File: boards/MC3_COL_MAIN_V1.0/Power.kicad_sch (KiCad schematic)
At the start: 6 parts, among them J3 SUPPLY_IN, Q1 AO4407C, U3 AMS1117-3.3

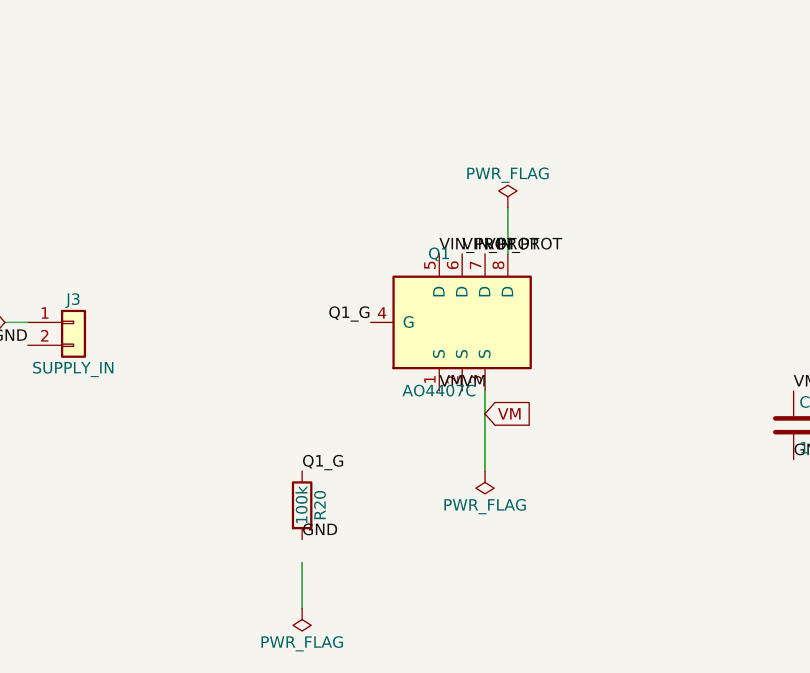
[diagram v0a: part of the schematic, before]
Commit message: Schematic: root sheet on-grid, I2C address straps as GND/+3V3 global labels, ERC clean (warnings only)
- Root: Power/MCU/Connectors + 4x MotorChannel instances on the 1.27 mm grid; sheet pins wired
  to EN/PH/IPROPI/RC_OUT/nFAULT_leafN global labels; A1/A0 straps leaf1 GND/GND, leaf2
  GND/+3V3, leaf3 +3V3/GND, leaf4 +3V3/+3V3 (PROVISIONAL)
- Connectors: removed a GND drop that shorted ENC_leaf4; VM on the FFCs as global labels
- Power: PWR_FLAGs placed on the pin ends (VIN_PROT, VM, GND)
- ERC (kicad-cli, all severities): 0 errors, 8 same_local_global_label warnings (intended)
- Reference designators still duplicated across the 4 channel instances: needs Annotate
  in eeschema (no CLI path)

Co-Authored-By: Claude Fable 5 <noreply@anthropic.com>
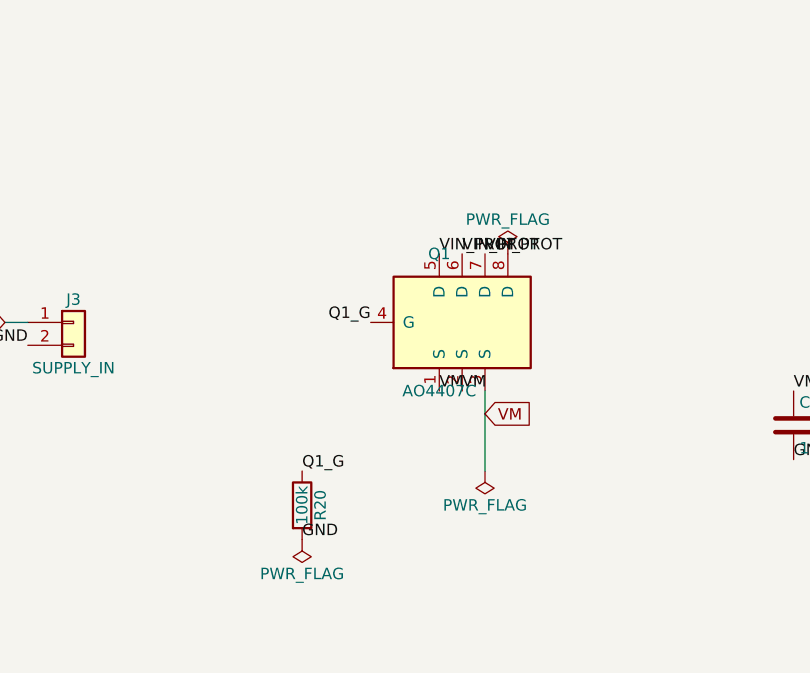
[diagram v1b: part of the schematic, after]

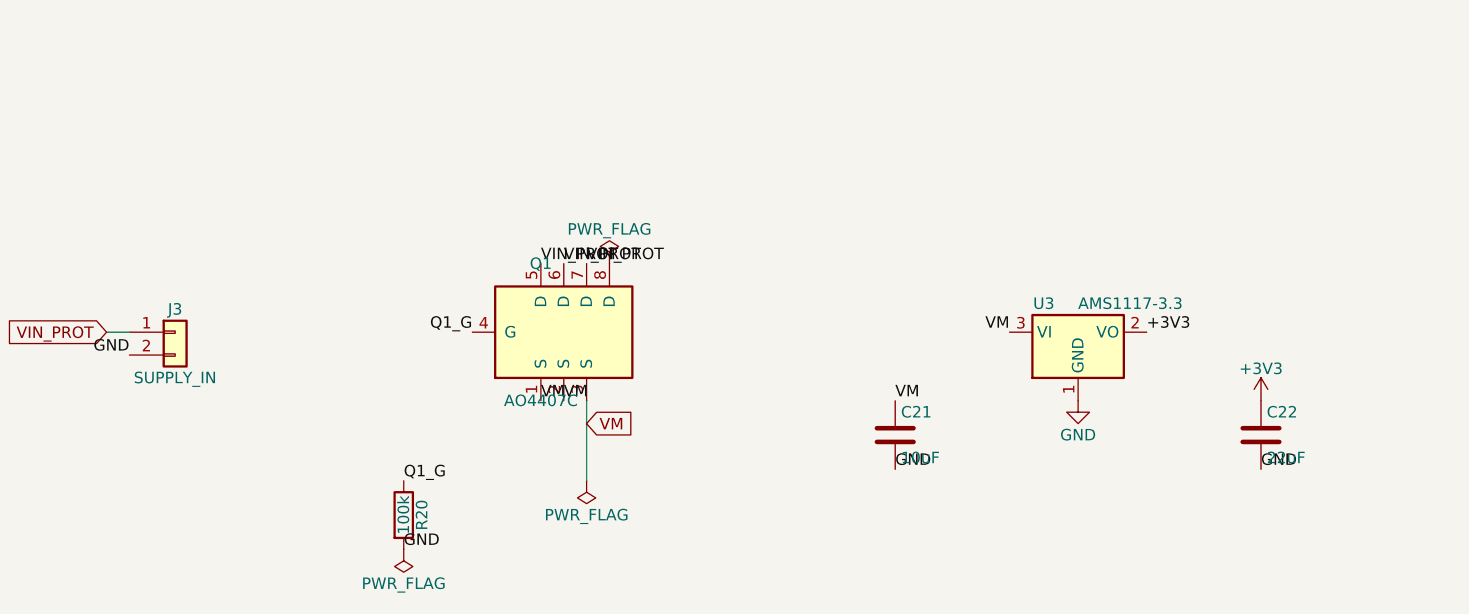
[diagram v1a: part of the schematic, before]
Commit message: Schematic annotated in eeschema (per-instance references for the 4 channel sheets); user review OK
Co-Authored-By: Claude Fable 5 <noreply@anthropic.com>
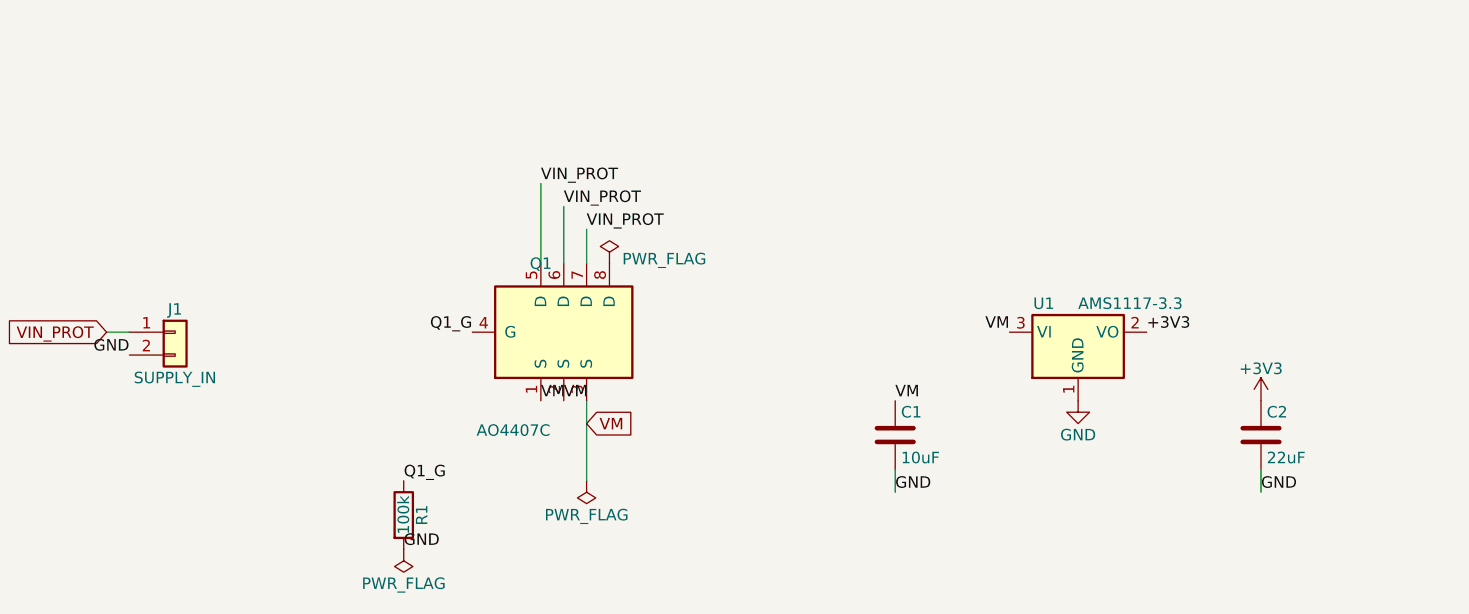
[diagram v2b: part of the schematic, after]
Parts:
- renumbered C21 to C1, C22 to C2, J3 to J1, R20 to R1, U3 to U1

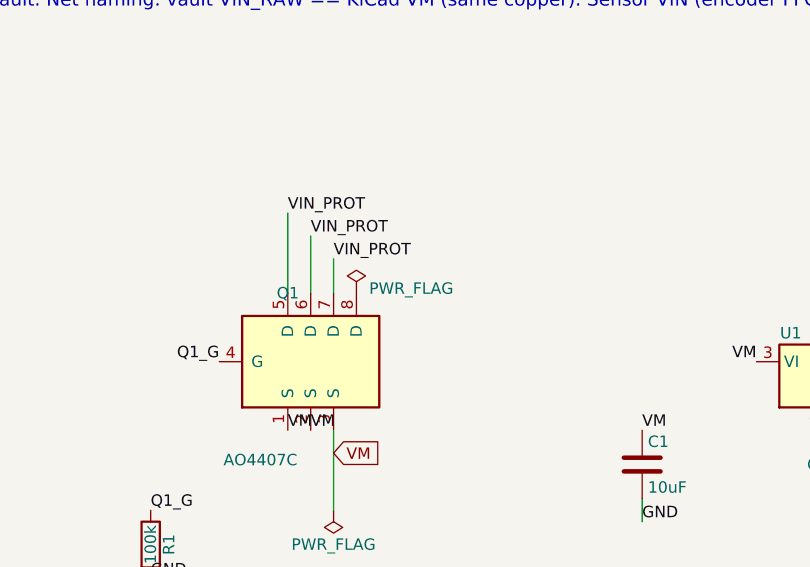
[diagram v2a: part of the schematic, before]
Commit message: Yaw channel fitted as 5th MotorChannel instance (user decision); Power VIN_PROT pin 8 labelled; MIGRATION status
- MCU: EN_yaw PA9, PH_yaw PB12, IPROPI_yaw PC4 (vault reserved pins); PROVISIONAL nFAULT_yaw
  PC12, RC_OUT_yaw PB13
- Root: sheet 'yaw' -> MotorChannel.kicad_sch, A1 open (Hi-Z), A0 GND
- ERC: 0 errors, same_local_global_label warnings only
- Needs re-annotation in eeschema for the new instance

Co-Authored-By: Claude Fable 5 <noreply@anthropic.com>
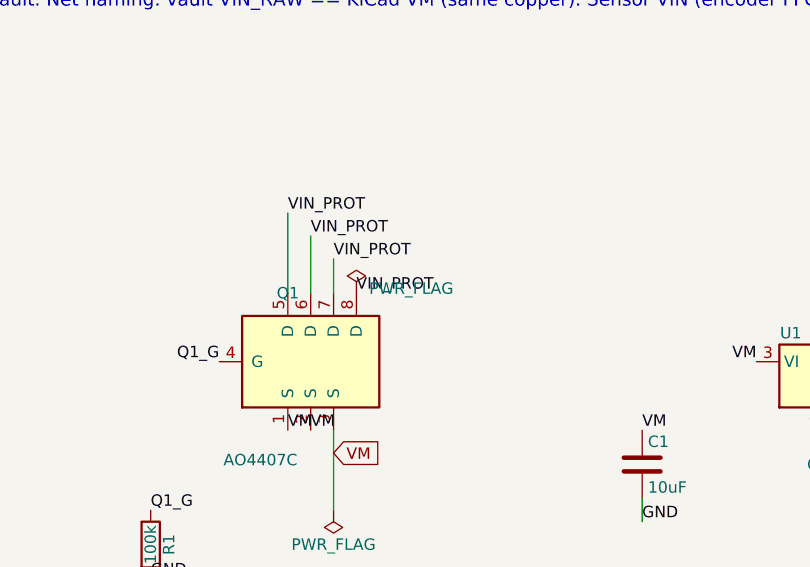
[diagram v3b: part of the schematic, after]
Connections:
- net VIN_PROT: now also Q1.8 (D)
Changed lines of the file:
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@@
 		)
 	)
+  (label "VIN_PROT"
+    (at 87.63000000000001 72.39 0)
+    (fields_autoplaced yes)
+    (effects (font (size 1.27 1.27)) (justify left bottom))
+  )
 	(symbol
 		(lib_id "Regulator_Linear:AMS1117-3.3")

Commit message: I2C address straps: high straps via 2.2k pull-ups R40-R43 (SLVSH04 Table 8-28 note); address table on root sheet
Co-Authored-By: Claude Fable 5 <noreply@anthropic.com>
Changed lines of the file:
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@@
+		)
+	)
+	(label "VIN_PROT"
+		(at 87.63 72.39 0)
+		(effects
+			(font
+				(size 1.27 1.27)
+			)
+			(justify left bottom)
 		)
 	)
@@
 		)
 	)
-  (label "VIN_PROT"
-    (at 87.63000000000001 72.39 0)
-    (fields_autoplaced yes)
-    (effects (font (size 1.27 1.27)) (justify left bottom))
-  )
 	(symbol
 		(lib_id "Regulator_Linear:AMS1117-3.3")

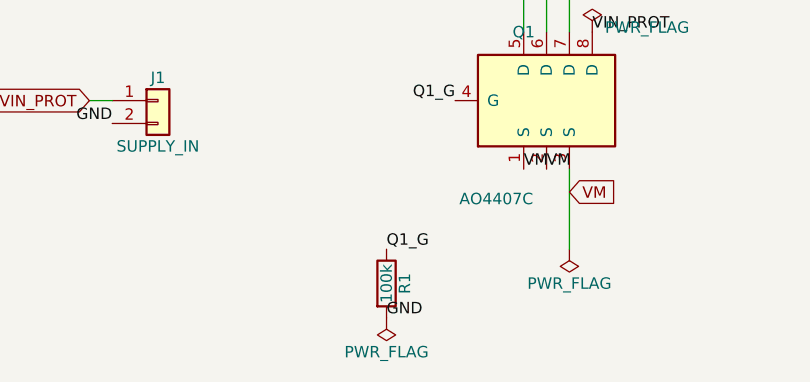
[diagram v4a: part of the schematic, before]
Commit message: Schematic re-annotated in eeschema after yaw channel + strap pull-ups
Co-Authored-By: Claude Fable 5 <noreply@anthropic.com>
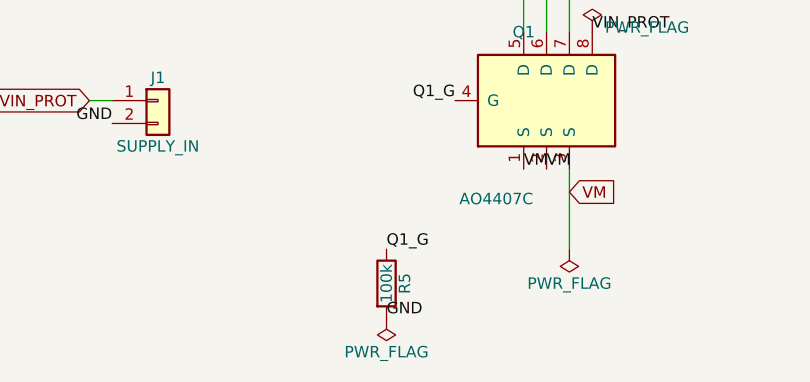
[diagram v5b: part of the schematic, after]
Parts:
- renumbered R1 to R5
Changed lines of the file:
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@@
 		(in_pos_files yes)
 		(dnp no)
-		(property "Reference" "R1"
+		(property "Reference" "R5"
 			(at 66.802 100.33 90)
 			(show_name no)
@@
 			(project "MC3_COL_MAIN_V1.0"
 				(path "/7d5f4202-d55e-4c7b-a2df-dd599db38e48/d6d9c27b-d616-4172-a586-88c2a3452975"
-					(reference "R1")
+					(reference "R5")
 					(unit 1)
 				)

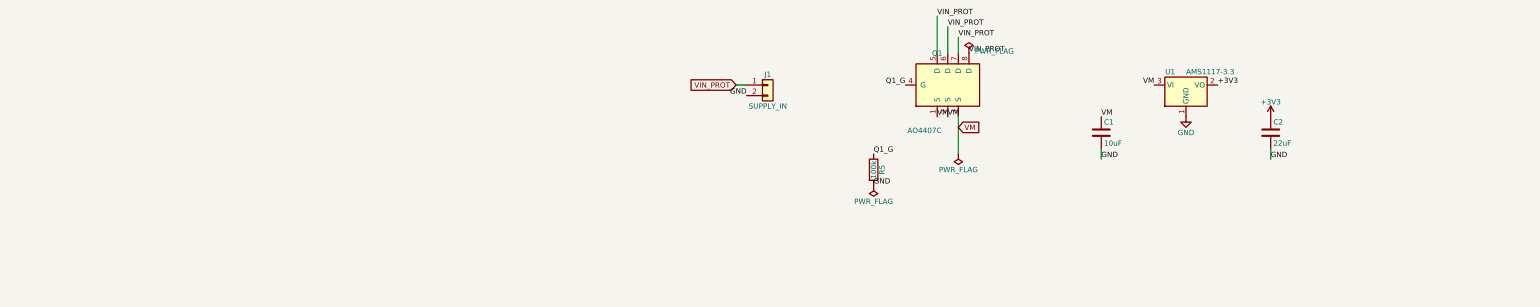
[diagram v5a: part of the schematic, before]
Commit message: Design review changes: HSE caps 33pF, R_IPROPI 6.8k (1.99 A trip), VM bulk, sensor rail filter, input fuse+TVS, NRST cap, 6-pin SWD with SWO, VDDA ferrite, LEDs, test points, tantalum LDO cap
- MCU: C6/C10 18pF -> 33pF (X32258MSB4SI is CL=20pF); C60 100nF on NRST; J2 -> Conn_01x06
  (+NRST, +SWO on PB3); VDDA split from +3V3 through FB60 + PWR_FLAG; heartbeat LED D60/R60
  on PA5, power LED D61/R61; test points TP60-64 (+3V3, SCL, SDA, IPROPI_leaf1, GND)
- Power: J1 -> VIN_PAD -> F60 polyfuse -> VIN_PROT; D62 SMAJ5.0A TVS VIN_PROT-GND; C61/C62
  2x22uF VM bulk; TP65 VM, TP66 VIN_PROT; C2 LDO output cap -> tantalum 22uF 10V (C_Polarized,
  CP_EIA-3216-18)
- Connectors: FFC VIN now VSENS = VM through FB61 + C63 4.7uF
- MotorChannel: R_IPROPI 8.45k -> 6.8k (I_TRIP = 3.3/(6.8k*244uA/A) = 1.99 A)
- Library: stock L_0603, D_SMA, Fuse_1206, CP_EIA-3216-18, TestPoint_Pad_1.0x1.0mm, LED_0603,
  PinHeader_1x06 footprints copied in
- ERC 0 errors (same_local_global_label warnings only); netlist walked

Co-Authored-By: Claude Fable 5 <noreply@anthropic.com>
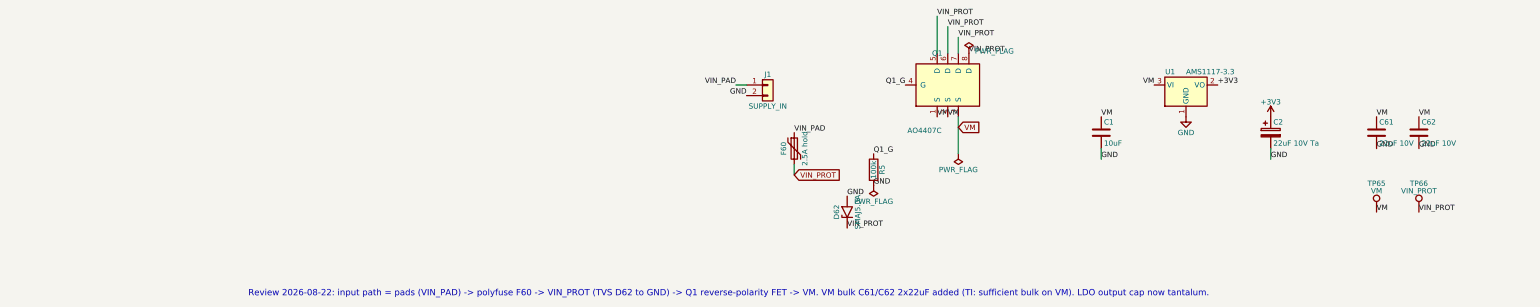
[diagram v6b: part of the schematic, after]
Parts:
- added C61, C62: 22uF 10V, MC3_COL_MAIN:C_0805_2012Metric, symbol Device:C
- added D62: SMAJ5.0A, MC3_COL_MAIN:D_SMA, symbol Diode:SMAJ5.0A
- added F60: 2.5A hold, MC3_COL_MAIN:Fuse_1206_3216Metric, symbol Device:Polyfuse
- added TP65: VM, MC3_COL_MAIN:TestPoint_Pad_1.0x1.0mm, symbol Connector:TestPoint
- added TP66: VIN_PROT, MC3_COL_MAIN:TestPoint_Pad_1.0x1.0mm, symbol Connector:TestPoint
- C2: value 22uF -> 22uF 10V Ta; footprint MC3_COL_MAIN:C_0805_2012Metric -> MC3_COL_MAIN:CP_EIA-3216-18_Kemet-A; symbol Device:C -> Device:C_Polarized; Note LDO output 22uF - AMS1117 compensation cap. OPEN (vault): d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 -> LDO output cap changed to TANTALUM 22uF 10V case A (3216) p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
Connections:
- net GND: now also C61.2, C62.2, D62.2 (A2)
- net VIN_PROT: now also D62.1 (A1), F60.2, TP66.1; no longer J1.1 (Pin_1)
- net VM: now also C61.1, C62.1, TP65.1
- new net VIN_PAD: F60.1, J1.1 (Pin_1)
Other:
- note added: "Review 2026-08-22: input path = pads (VIN_PAD) -> polyfuse F60 -> VIN_PROT (TVS D62 to GND) -> Q1 reverse-polarity FET -> VM. VM bulk C61/C62 2x22uF added (TI: sufficient bulk on VM). LDO output cap now tantalum."

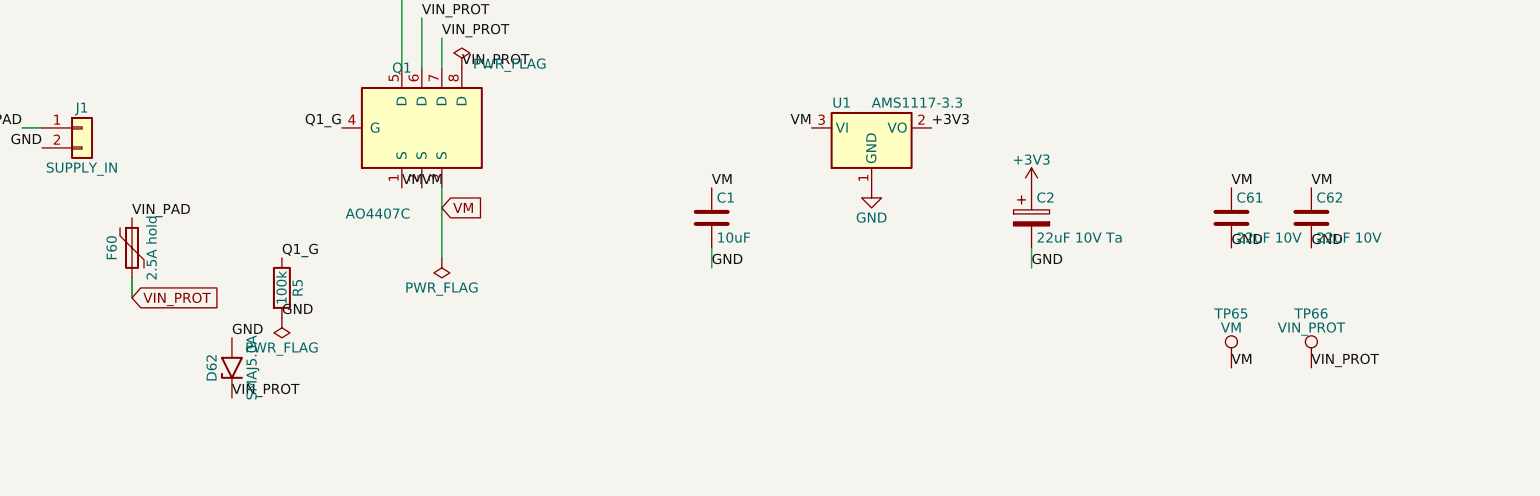
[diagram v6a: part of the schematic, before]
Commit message: LCSC/MPN fields on every support part (verified against the JLCPCB DB); R_IPROPI 6.8k = C93940; polyfuse 1206L200/12NR; MIGRATION register
Co-Authored-By: Claude Fable 5 <noreply@anthropic.com>
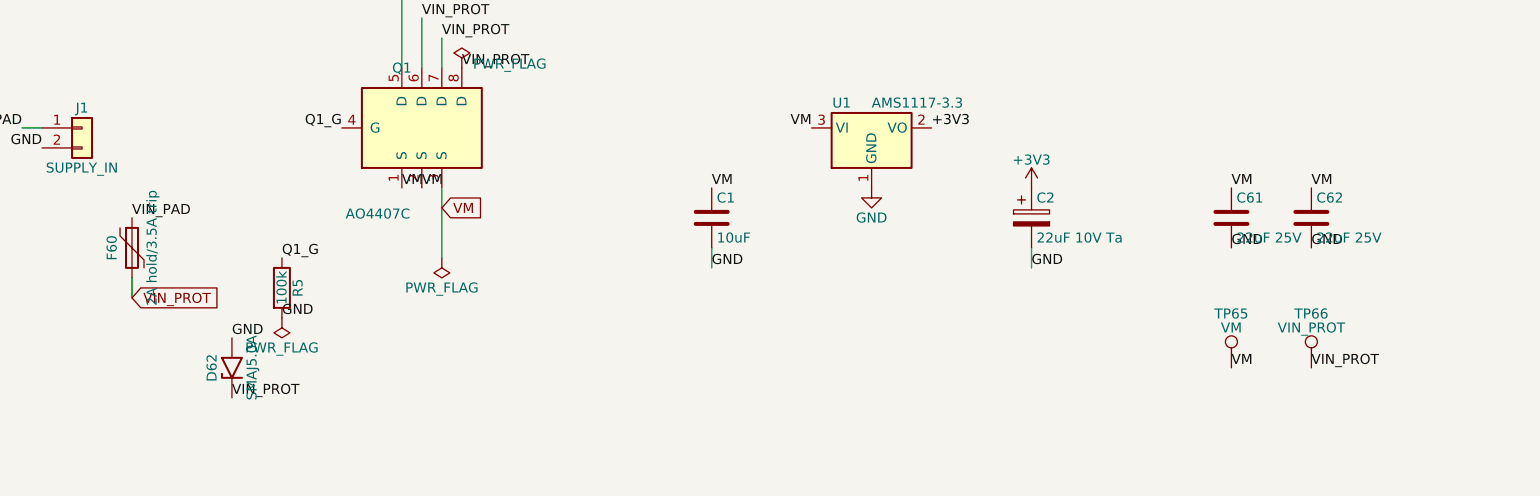
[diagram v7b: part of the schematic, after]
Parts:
- C1: LCSC (none) -> C15850; MPN (none) -> CL21A106KAYNNNE
- C2: LCSC (none) -> C11366; MPN (none) -> TAJA226K010RNJ
- C61, C62: value 22uF 10V -> 22uF 25V; LCSC (none) -> C45783; MPN (none) -> CL21A226MAQNNNE
- D62: LCSC (none) -> C78401; MPN (none) -> SMAJ5.0A/TR13
- F60: value 2.5A hold -> 2A hold/3.5A trip; LCSC (none) -> C19078716; MPN (none) -> 1206L200/12NR
- R5: LCSC (none) -> C25741; MPN (none) -> 0402WGF1003TCE
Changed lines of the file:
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@@
 			)
 		)
-	)
+		(property "LCSC" "C15850"
+			(at 119.38 91.44 0)
+			(hide yes)
+			(effects
+				(font
+					(size 1.27 1.27)
+				)
+			)
+		)
+		(property "MPN" "CL21A106KAYNNNE"
+			(at 119.38 91.44 0)
+			(hide yes)
+			(effects
+				(font
+					(size 1.27 1.27)
+				)
+			)
+		))
 	(symbol
 		(lib_id "power:+3V3")
@@
 			)
 		)
-	)
+		(property "LCSC" "C25741"
+			(at 64.77 100.33 0)
+			(hide yes)
+			(effects
+				(font
+					(size 1.27 1.27)
+				)
+			)
+		)
+		(property "MPN" "0402WGF1003TCE"
+			(at 64.77 100.33 0)
+			(hide yes)
+			(effects
+				(font
+					(size 1.27 1.27)
+				)
+			)
+		))
 	(symbol
 		(lib_id "Connector_Generic:Conn_01x02")
@@
 			)
 		)
-	)
+		(property "LCSC" "C11366"
+			(at 160.02 91.44 0)
+			(hide yes)
+			(effects
+				(font
+					(size 1.27 1.27)
+				)
+			)
+		)
+		(property "MPN" "TAJA226K010RNJ"
+			(at 160.02 91.44 0)
+			(hide yes)
+			(effects
+				(font
+					(size 1.27 1.27)
+				)
+			)
+		))
 	(symbol
 		(lib_id "power:PWR_FLAG")
@@
 			)
 		)
-		(property "Value" "2.5A hold"
+		(property "Value" "2A hold/3.5A trip"
 			(at 48.26 95.25 90)
 			(effects
@@
 				)
 			)
+		)
+		(property "LCSC" "C19078716"
+			(at 45.72 95.25 0)
+			(hide yes)
+			(effects
+				(font
+					(size 1.27 1.27)
+				)
+			)
+		)
+		(property "MPN" "1206L200/12NR"
+			(at 45.72 95.25 0)
+			(hide yes)
+			(effects
+				(font
+					(size 1.27 1.27)
+				)
+			)
 		))
 	(symbol
@@
 				)
 			)
+		)
+		(property "LCSC" "C78401"
+			(at 58.42 110.49 0)
+			(hide yes)
+			(effects
+				(font
+					(size 1.27 1.27)
+				)
+			)
+		)
+		(property "MPN" "SMAJ5.0A/TR13"
+			(at 58.42 110.49 0)
+			(hide yes)
+			(effects
+				(font
+					(size 1.27 1.27)
+				)
+			)
 		))
 	(symbol
@@
 			)
 		)
-		(property "Value" "22uF 10V"
+		(property "Value" "22uF 25V"
 			(at 186.055 93.98 0)
 			(effects
@@
 				)
 			)
+		)
+		(property "LCSC" "C45783"
+			(at 185.42 91.44 0)
+			(hide yes)
+			(effects
+				(font
+					(size 1.27 1.27)
+				)
+			)
+		)
+		(property "MPN" "CL21A226MAQNNNE"
+			(at 185.42 91.44 0)
+			(hide yes)
+			(effects
+				(font
+					(size 1.27 1.27)
+				)
+			)
 		))
 	(symbol
@@
 			)
 		)
-		(property "Value" "22uF 10V"
+		(property "Value" "22uF 25V"
 			(at 196.215 93.98 0)
 			(effects
@@
 			(at 195.58 91.44 0)
 			(hide yes)
+			(effects
+				(font
+					(size 1.27 1.27)
+				)
+			)
+		)
+		(property "LCSC" "C45783"
+			(at 195.58 91.44 0)
+			(hide yes)
+			(effects
+				(font
+					(size 1.27 1.27)
+				)
+			)
+		)
+		(property "MPN" "CL21A226MAQNNNE"
+			(at 195.58 91.44 0)
+			(hide yes)
